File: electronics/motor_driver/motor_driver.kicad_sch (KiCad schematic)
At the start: 83 parts, among them J1 Power, J2 Control, J3 Motor, Q1 FDD86381, Q2 FDD86381, Q3 FDD86381, Q4 FDD86381, U1 SY8502, U2 L78L05_SOT89, U3 LTV-356T, U4 TLP2270, U5 L6393, U6 L6393, U7 LTV-356T

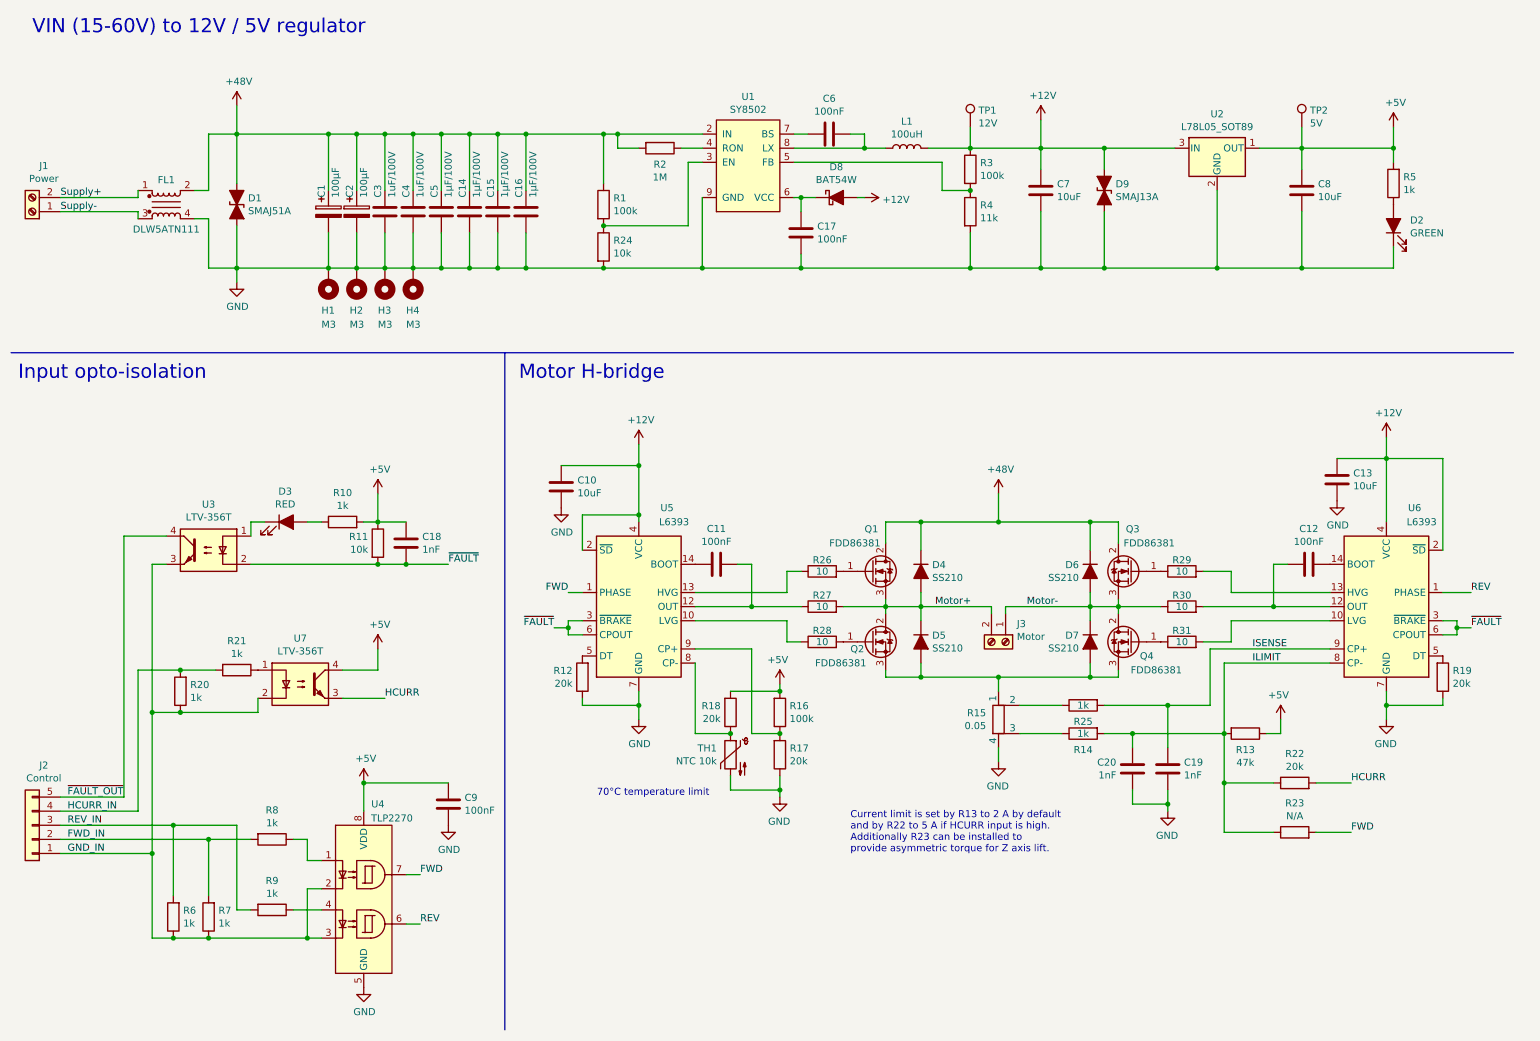
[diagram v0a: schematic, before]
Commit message: Update wiring diagram & motor driver part values
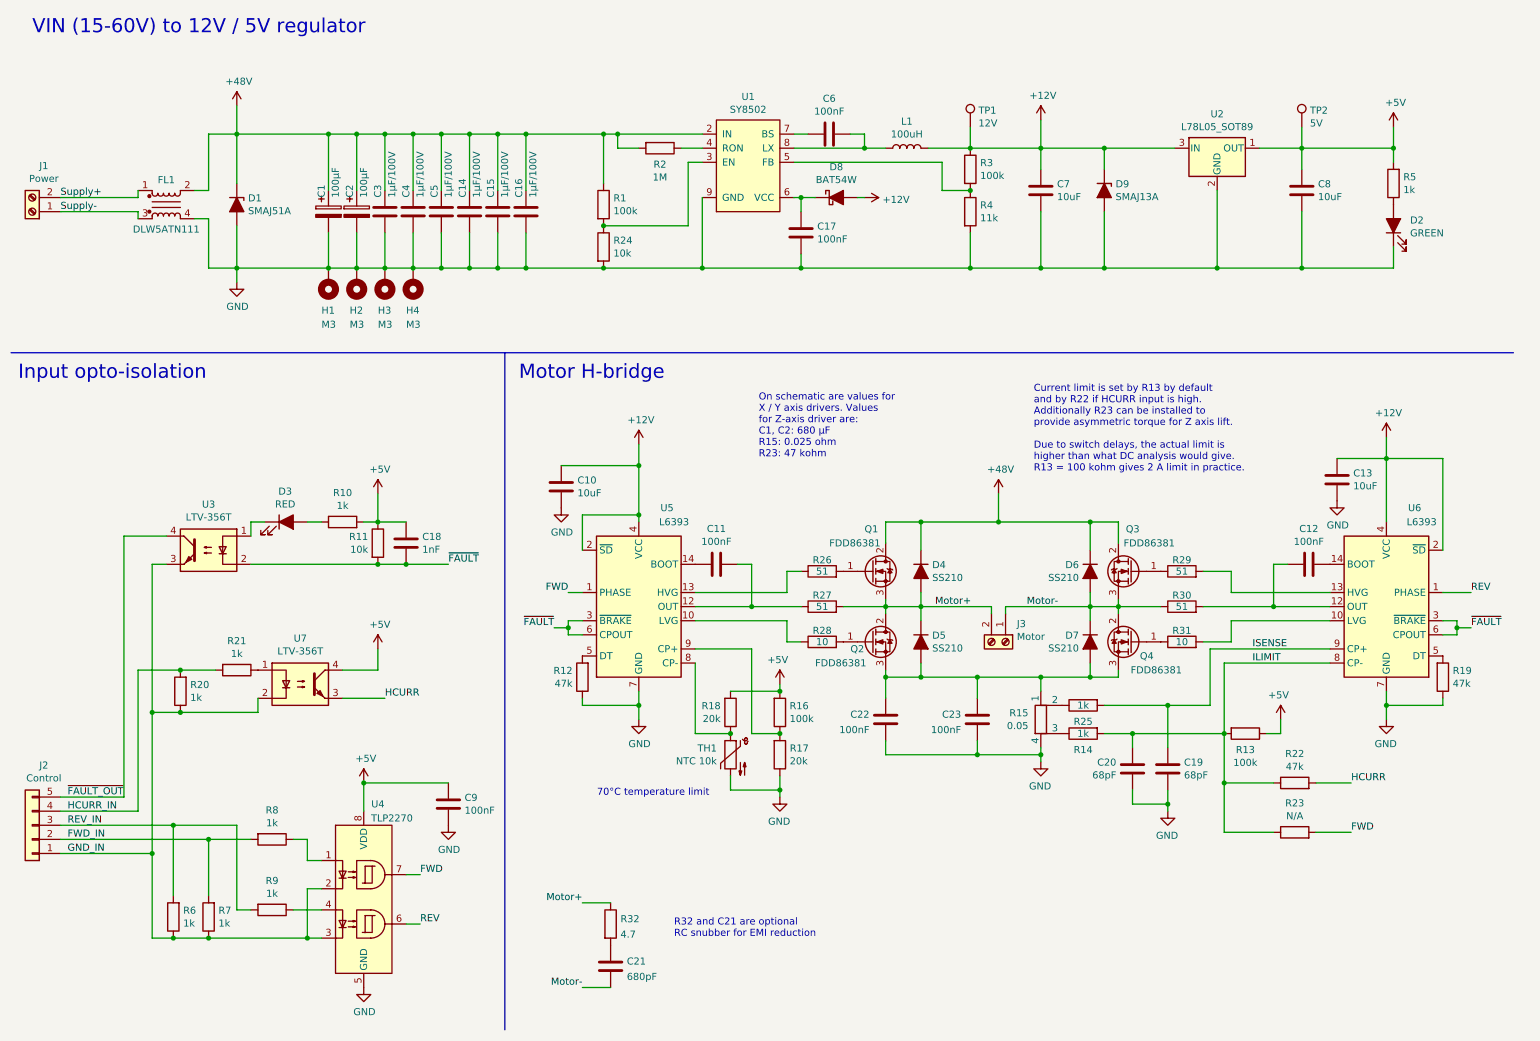
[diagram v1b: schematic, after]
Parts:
- added C21: 680pF, Capacitor_SMD:C_0805_2012Metric, symbol Device:C
- added C22, C23: 100nF, Capacitor_SMD:C_0603_1608Metric, symbol Device:C
- added R32: 4.7, Resistor_SMD:R_0805_2012Metric, symbol Device:R
- C19, C20: value 1nF -> 68pF
- C3, C4: value 1uF/100V -> 1µF/100V
- D1, D9: symbol Device:D_TVS_ALT -> Device:D_Zener_Filled
- R12, R19, R22: value 20k -> 47k
- R13: value 47k -> 100k
- R26, R27, R29, R30: value 10 -> 51
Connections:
- net GND: now also C22.2, C23.2
- net Motor+: now also R32.1
- net Motor-: now also C21.2
- net at D5.2 (A), D7.2 (A), Q2.3 (S)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: now also C22.1, C23.1
- new net: C21.1, R32.2
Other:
- note added: "Current limit is set by R13 by default and by R22 if HCURR input is high. Additionally R23 can be installed to provide asymmetric torque for Z axis lift. Due to switch delays, the actual limit is higher than what DC analysis would give. R13 = 100 kohm gives 2 A limit in practice."
- note added: "On schematic are values for X / Y axis drivers. Values for Z-axis driver are: C1, C2: 680 µF R15: 0.025 ohm R23: 47 kohm"
- note added: "R32 and C21 are optional RC snubber for EMI reduction"
- note removed: "Current limit is set by R13 to 2 A by default and by R22 to 5 A if HCURR input is high. Additionally R23 can be installed to provide asymmetric torque for Z axis lift."
- moved on the sheet: R15
